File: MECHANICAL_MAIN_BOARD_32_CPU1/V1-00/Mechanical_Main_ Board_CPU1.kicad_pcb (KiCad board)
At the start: 2 copper layers, 88.9 x 220.6 mm, 172 parts, among them J1 RJ12, K1 CONN_3, K10 COLONETTE, K11 COLONETTE, K12 COLONETTE, K13 COLONETTE, K2 CONN_3, K3 CONN_3, K4 CONN_3, K5 CONN_3, K6 CONN_3, K7 CONN_3, K8 CONN_3, K9 CONN_3, P1 CONN_8X2, P1001 CONN_13X2, P1002 CONN_8X2, P2 CONN_8X2, P3 CONN_13X2, P4 CONN_5X2, P5 CONN_4, P6 CONN_4, P7 CONN_4, P8 CONN_4, P9 CONN_4, Q1 2N7002, Q10 2N7002, Q11 2N7002, Q12 2N7002, Q2 2N7002, Q3 2N7002, Q4 2N7002, Q5 2N7002, Q6 2N7002, Q7 2N7002, Q8 2N7002, Q9 2N7002, SW1 SW_PUSH_SMALL, U1 PIC32MX795F512H, U2 24C512, U3 PCA9306, U4 PCA9306, X1 32,768k

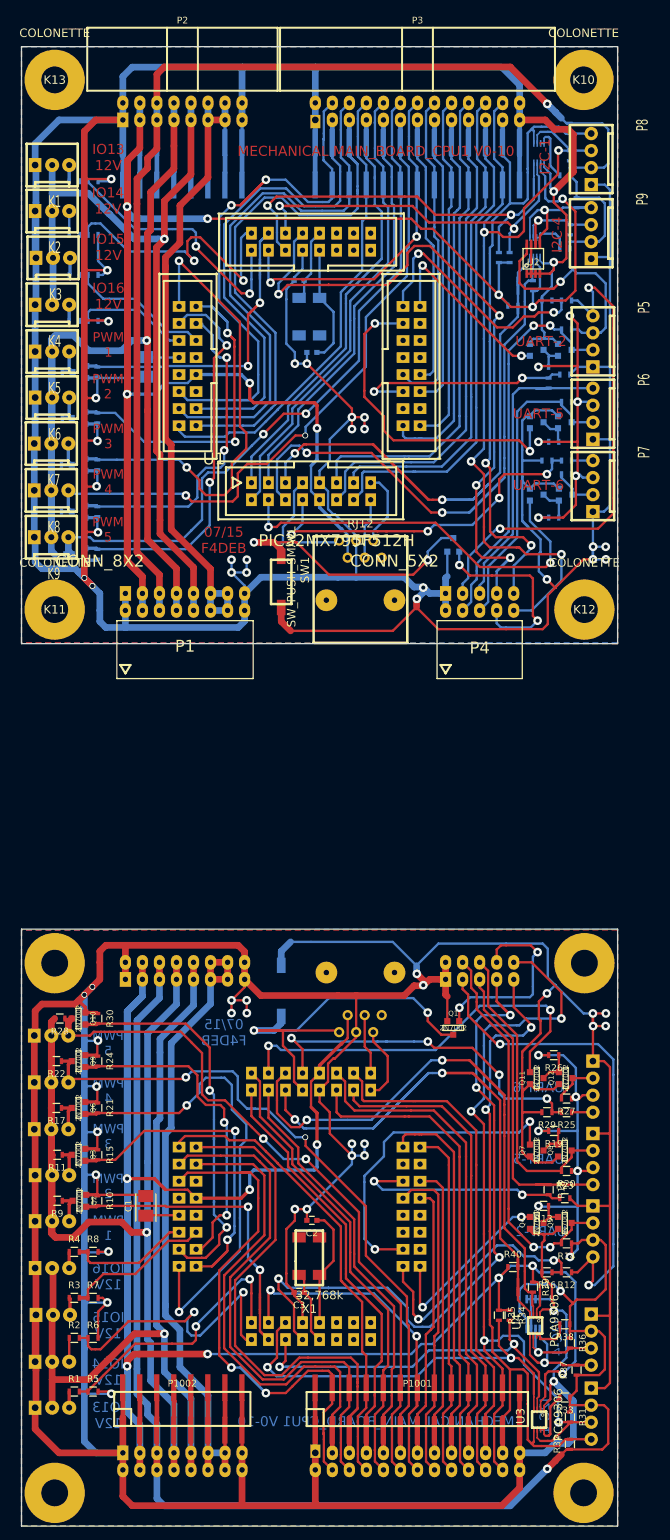
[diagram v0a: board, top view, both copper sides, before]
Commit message: test mechanicalmotorboard PCB NOK
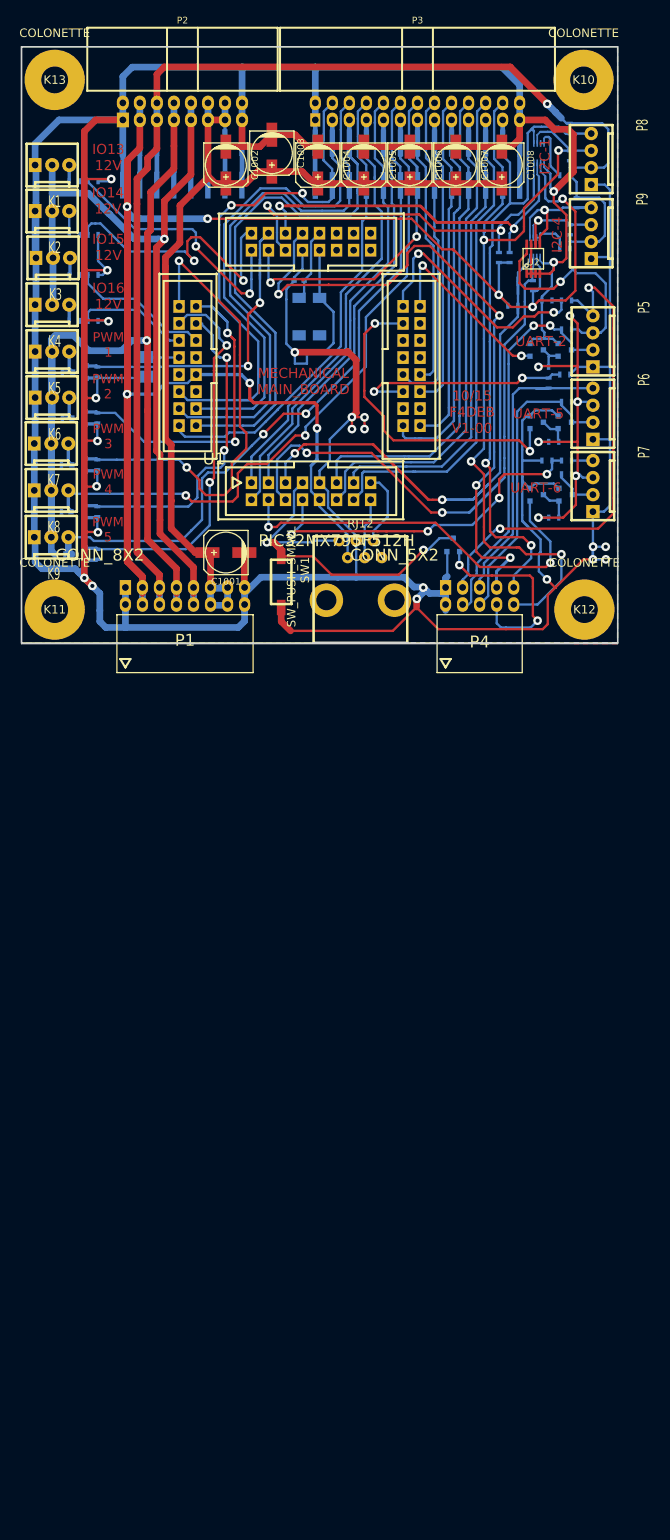
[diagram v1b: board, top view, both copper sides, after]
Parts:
- removed the C1 at (82.5, 207.8)
- removed the C2 at (107.3, 210.0)
- removed the C3 at (105.4, 220.7)
- removed the J1 at (114.6, 181.9)
- removed the K1 at (71.1, 237.9)
- removed the K10 at (147.8, 250.6)
- removed the K11 at (69.0, 171.6)
- removed the K12 at (148.0, 171.6)
- removed the K13 at (69.0, 250.6)
- removed the K2 at (71.1, 231.0)
- removed the K3 at (71.2, 224.1)
- removed the K4 at (71.1, 217.1)
- removed the K5 at (71.1, 210.1)
- removed the K6 at (71.1, 203.2)
- removed the K7 at (71.0, 196.4)
- removed the K8 at (71.0, 189.4)
- removed the K9 at (71.0, 182.4)
- removed the P1 at (98.8, 170.0)
- removed the P1001 at (123.0, 238.1)
- removed the P1002 at (88.0, 238.1)
- removed the P2 at (88.0, 251.0)
- removed the P3 at (123.1, 251.0)
- removed the P4 at (132.3, 172.7)
- removed the P5 at (149.2, 215.4)
- removed the P6 at (149.2, 204.6)
- removed the P7 at (149.2, 193.8)
- removed the P8 at (149.0, 242.6)
- removed the P9 at (149.0, 231.5)
- removed the Q1 at (128.4, 181.3)
- removed the Q10 at (72.5, 179.9)
- removed the Q11 at (140.8, 188.7)
- removed the Q12 at (145.2, 188.7)
- removed the Q2 at (72.6, 207.0)
- removed the Q3 at (72.5, 200.2)
- removed the Q4 at (140.8, 210.3)
- removed the Q5 at (145.0, 210.3)
- removed the Q6 at (72.5, 193.2)
- removed the Q7 at (140.8, 199.5)
- removed the Q8 at (145.0, 199.5)
- removed the Q9 at (72.5, 186.2)
- removed the R1 at (71.9, 235.5)
- removed the R10 at (75.3, 207.0)
- removed the R11 at (69.3, 200.2)
- removed the R12 at (145.3, 217.7)
- removed the R13 at (141.9, 207.8)
- removed the R14 at (145.3, 213.4)
- removed the R15 at (75.3, 200.2)
- removed the R16 at (142.4, 217.7)
- removed the R17 at (69.2, 193.2)
- removed the R18 at (142.6, 205.4)
- removed the R19 at (143.4, 196.6)
- removed the R2 at (71.9, 227.5)
- removed the R20 at (145.3, 202.6)
- removed the R21 at (75.3, 193.2)
- removed the R22 at (69.2, 186.2)
- removed the R23 at (145.0, 206.7)
- removed the R24 at (75.3, 186.2)
- removed the R25 at (145.3, 193.8)
- removed the R26 at (143.4, 185.3)
- removed the R27 at (145.3, 191.8)
- removed the R28 at (69.7, 179.9)
- removed the R29 at (142.4, 193.8)
- removed the R3 at (71.9, 221.5)
- removed the R30 at (75.3, 179.9)
- removed the R31 at (145.8, 239.3)
- removed the R32 at (145.8, 243.4)
- removed the R33 at (145.0, 236.4)
- removed the R34 at (136.8, 224.1)
- removed the R35 at (135.2, 224.1)
- removed the R36 at (145.8, 228.2)
- removed the R37 at (146.8, 232.3)
- removed the R38 at (145.0, 225.5)
- removed the R39 at (140.3, 219.9)
- removed the R4 at (71.9, 214.7)
- removed the R40 at (137.3, 216.9)
- removed the R5 at (74.7, 235.5)
- removed the R6 at (74.7, 227.5)
- removed the R7 at (74.7, 221.5)
- removed the R8 at (74.7, 214.7)
- removed the R9 at (69.3, 207.0)
- removed the SW1 at (102.7, 179.5)
- removed the U1 at (98.3, 188.0)
- removed the U2 at (140.3, 223.9)
- removed the U3 at (141.2, 239.7)
- removed the U4 at (140.6, 225.7)
- removed the X1 at (108.5, 218.1)
- added C1001: CP, Capacitors_SMD:c_elec_6.3x7.7, F.Cu at (94.5, 110.4)
- added C1002: CP, Capacitors_SMD:c_elec_6.3x7.7, F.Cu at (94.5, 52.6)
- added C1003: CP, Capacitors_SMD:c_elec_6.3x7.7, F.Cu at (101.3, 50.8)
- added C1004: CP, Capacitors_SMD:c_elec_6.3x7.7, F.Cu at (108.2, 52.6)
- added C1005: CP, Capacitors_SMD:c_elec_6.3x7.7, F.Cu at (115.1, 52.6)
- added C1006: CP, Capacitors_SMD:c_elec_6.3x7.7, F.Cu at (121.9, 52.6)
- added C1007: CP, Capacitors_SMD:c_elec_6.3x7.7, F.Cu at (128.8, 52.6)
- added C1008: CP, Capacitors_SMD:c_elec_6.3x7.7, F.Cu at (135.6, 52.6)
- Q1, Q10, Q11, Q12, Q2, Q3, Q4, Q5, Q6, Q7, Q8, Q9: footprint f4deb-mod-library:SOT23GDS -> Housings_SOT-23_SOT-143_TSOT-6:SOT-23
- moved P1 0.89 mm to (98.8, 119.6)
- moved P4 0.89 mm to (132.3, 116.8)
- moved Q9 0.13 mm to (72.4, 104.3), turned to 270 degrees
- moved P1001 0.08 mm to (123.1, 52.5)
- turned Q1 to 180 degrees
- turned Q10 to 270 degrees
- turned Q11 to 90 degrees
- turned Q12 to 90 degrees
- turned Q2 to 270 degrees
- turned Q3 to 270 degrees
- turned Q4 to 90 degrees
- turned Q5 to 90 degrees
- turned Q6 to 270 degrees
- turned Q7 to 90 degrees
- turned Q8 to 90 degrees
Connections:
- P4 pad 8: (no net) -> /RST
- R13 pad 1: (no net) -> Net-(Q4-Pad3)
- R19 pad 1: (no net) -> Net-(Q7-Pad3)
- R26 pad 1: (no net) -> Net-(Q11-Pad3)
- U1 pad 29: (no net) -> /TX5
- U1 pad 32: (no net) -> /TX2
- U1 pad 4: (no net) -> /TX6
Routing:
- net GND: track 1538.6 -> 828.7 mm, vias 56 -> 23
- net (no net): track 359.0 -> 0.00 mm, vias 16 -> 0
- net +3V3: track 652.5 -> 326.2 mm, vias 16 -> 8
- net +5VD: track 589.3 -> 294.7 mm, vias 16 -> 8
- net +5V: track 338.6 -> 169.3 mm, vias 2 -> 1
- net +12V: track 256.9 -> 128.4 mm, vias 2 -> 1
- net /SCL1-5V: track 256.0 -> 127.6 mm, vias 8 -> 4
- net /SDA1-5V: track 217.1 -> 107.7 mm, vias 4 -> 2
- net /OC4-5V: track 212.4 -> 106.2 mm, vias 4 -> 2
- net /OC5-5V: track 207.6 -> 103.8 mm, vias 4 -> 2
- net /SDA4: track 207.3 -> 103.7 mm, vias 4 -> 2
- net /INT1: track 206.2 -> 108.4 mm, vias 8 -> 4
- net /SCL4: track 183.7 -> 91.9 mm, vias 4 -> 2
- net /IO18: track 168.6 -> 77.5 mm, vias 4 -> 2
- net /RSTA: track 150.6 -> 61.2 mm, vias 4 -> 2
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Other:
- board size 88.9 x 220.6 mm -> 88.9 x 89 mm
- board text added: "10/15 F4DEB V1-00"
- board text added: "MECHANICAL MAIN_BOARD"
- board text removed: "07/15 F4DEB"
- board text removed: "MECHANICAL MAIN_BOARD_CPU1 V0-10"
